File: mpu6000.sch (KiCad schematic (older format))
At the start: 4 parts, among them U3 MPU-6000

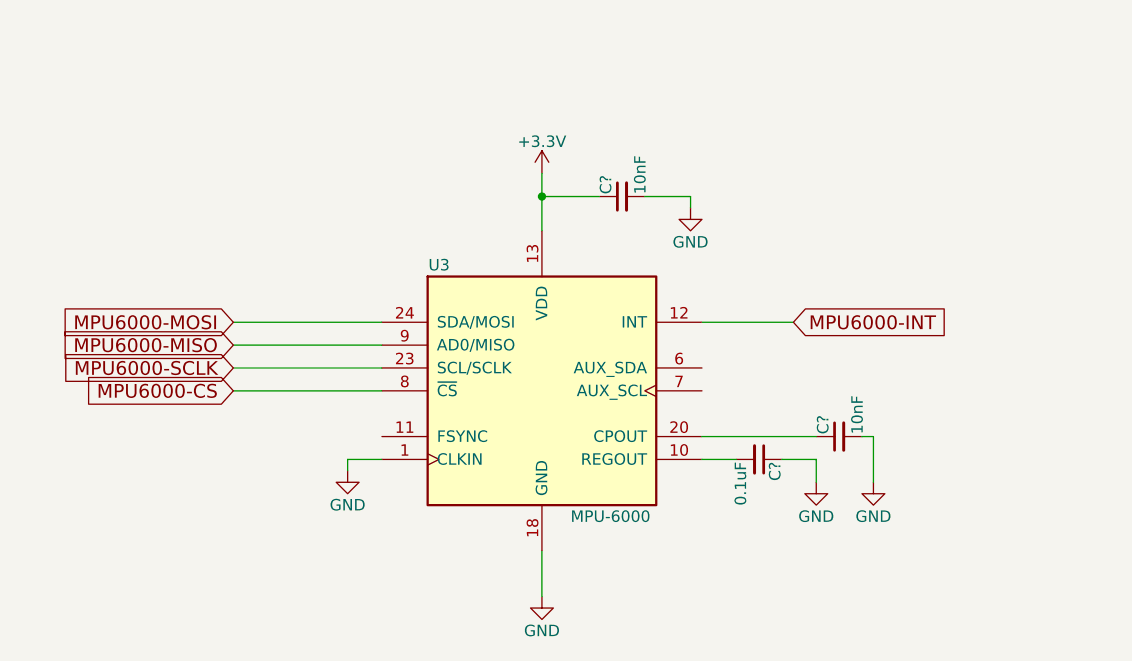
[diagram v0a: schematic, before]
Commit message: Moved LEDs to new sheet
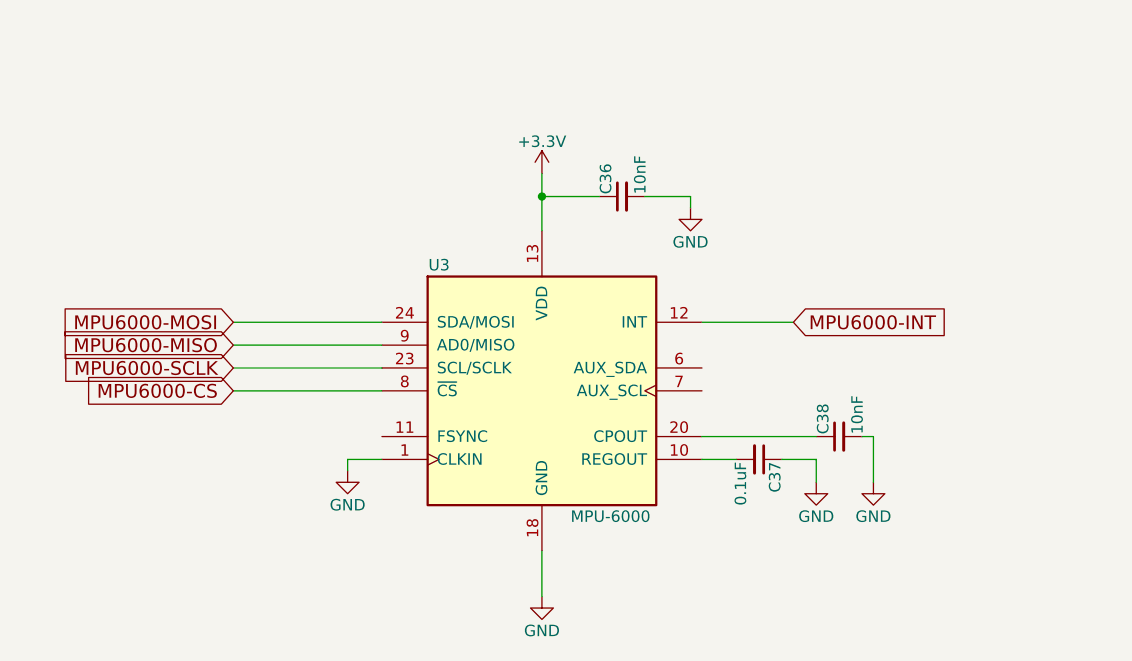
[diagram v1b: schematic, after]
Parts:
- gave numbers to parts that had none: 3
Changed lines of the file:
@@
 $Descr A4 11693 8268
 encoding utf-8
-Sheet 4 5
+Sheet 4 6
 Title ""
 Date ""
@@
 	7050 3500 6650 3500
 $Comp
-L +3.3V #PWR?
+L +3.3V #PWR1242
 U 1 1 5B360D5D
 P 5950 2850
-F 0 "#PWR?" H 5950 2700 50  0001 C CNN
+F 0 "#PWR1242" H 5950 2700 50  0001 C CNN
 F 1 "+3.3V" H 5950 2990 50  0000 C CNN
 F 2 "" H 5950 2850 50  0001 C CNN
@@
 $EndComp
 $Comp
-L GND #PWR?
+L GND #PWR1243
 U 1 1 5B360D77
 P 5950 4700
-F 0 "#PWR?" H 5950 4450 50  0001 C CNN
+F 0 "#PWR1243" H 5950 4450 50  0001 C CNN
 F 1 "GND" H 5950 4550 50  0000 C CNN
 F 2 "" H 5950 4700 50  0001 C CNN
@@
 	5950 2850 5950 3100
 $Comp
-L GND #PWR?
+L GND #PWR1246
 U 1 1 5B360DB0
 P 7400 4200
-F 0 "#PWR?" H 7400 3950 50  0001 C CNN
+F 0 "#PWR1246" H 7400 3950 50  0001 C CNN
 F 1 "GND" H 7400 4050 50  0000 C CNN
 F 2 "" H 7400 4200 50  0001 C CNN
@@
 $EndComp
 $Comp
-L GND #PWR?
+L GND #PWR1245
 U 1 1 5B360DCD
 P 7150 4200
-F 0 "#PWR?" H 7150 3950 50  0001 C CNN
+F 0 "#PWR1245" H 7150 3950 50  0001 C CNN
 F 1 "GND" H 7150 4050 50  0000 C CNN
 F 2 "" H 7150 4200 50  0001 C CNN
@@
 $EndComp
 $Comp
-L C_Small C?
+L C_Small C37
 U 1 1 5B360DDD
 P 6900 4100
-F 0 "C?" H 6910 4170 50  0000 L CNN
+F 0 "C37" H 6910 4170 50  0000 L CNN
 F 1 "0.1uF" H 6910 4020 50  0000 L CNN
 F 2 "" H 6900 4100 50  0001 C CNN
@@
 $EndComp
 $Comp
-L C_Small C?
+L C_Small C38
 U 1 1 5B360E5E
 P 7250 4000
-F 0 "C?" H 7260 4070 50  0000 L CNN
+F 0 "C38" H 7260 4070 50  0000 L CNN
 F 1 "10nF" H 7260 3920 50  0000 L CNN
 F 2 "" H 7250 4000 50  0001 C CNN
@@
 	7150 4100 7150 4200
 $Comp
-L C_Small C?
+L C_Small C36
 U 1 1 5B361055
 P 6300 2950
-F 0 "C?" H 6310 3020 50  0000 L CNN
+F 0 "C36" H 6310 3020 50  0000 L CNN
 F 1 "10nF" H 6310 2870 50  0000 L CNN
 F 2 "" H 6300 2950 50  0001 C CNN
@@
 $EndComp
 $Comp
-L GND #PWR?
+L GND #PWR1244
 U 1 1 5B3610B5
 P 6600 3000
-F 0 "#PWR?" H 6600 2750 50  0001 C CNN
+F 0 "#PWR1244" H 6600 2750 50  0001 C CNN
 F 1 "GND" H 6600 2850 50  0000 C CNN
 F 2 "" H 6600 3000 50  0001 C CNN
@@
 	6600 2950 6600 3000
 $Comp
-L GND #PWR?
+L GND #PWR1241
 U 1 1 5B3610F5
 P 5100 4150
-F 0 "#PWR?" H 5100 3900 50  0001 C CNN
+F 0 "#PWR1241" H 5100 3900 50  0001 C CNN
 F 1 "GND" H 5100 4000 50  0000 C CNN
 F 2 "" H 5100 4150 50  0001 C CNN

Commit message: zone movement + routing of all circuits
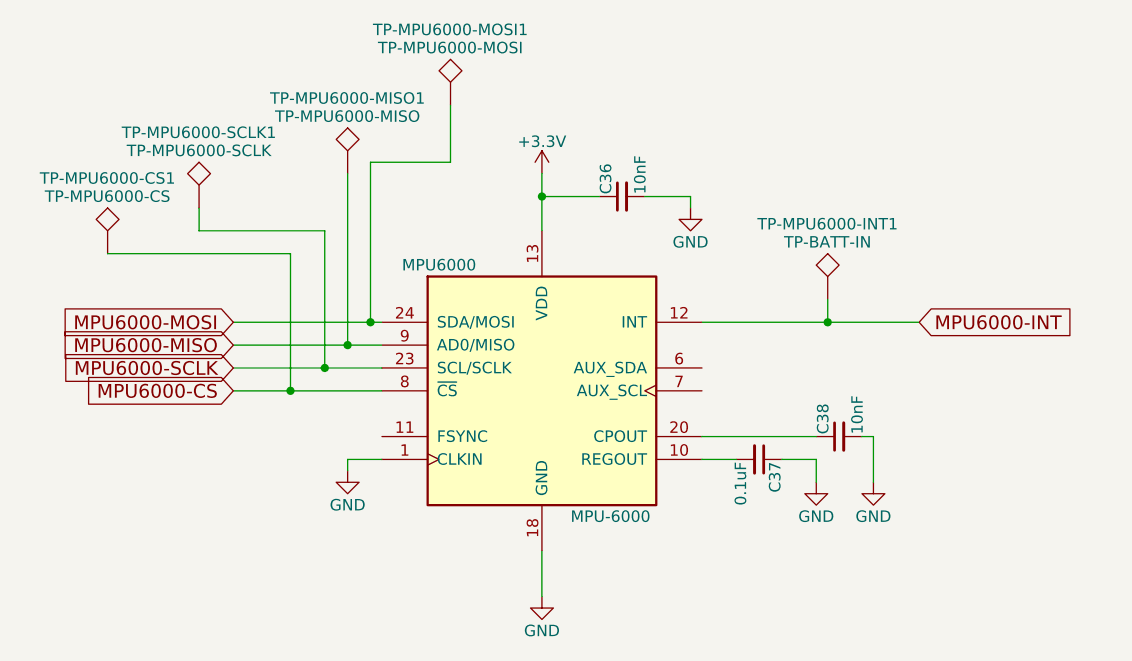
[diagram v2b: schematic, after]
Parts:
- added TP-MPU6000-CS1: TP-MPU6000-CS, Measurement_Points:Measurement_Point_Round-SMD-Pad_Small, symbol TEST
- added TP-MPU6000-INT1: TP-BATT-IN, Measurement_Points:Measurement_Point_Round-SMD-Pad_Small, symbol TEST
- added TP-MPU6000-MISO1: TP-MPU6000-MISO, Measurement_Points:Measurement_Point_Round-SMD-Pad_Small, symbol TEST
- added TP-MPU6000-MOSI1: TP-MPU6000-MOSI, Measurement_Points:Measurement_Point_Round-SMD-Pad_Small, symbol TEST
- added TP-MPU6000-SCLK1: TP-MPU6000-SCLK, Measurement_Points:Measurement_Point_Round-SMD-Pad_Small, symbol TEST
- C36, C37, C38: footprint (none) -> Capacitors_SMD:C_0603
- renumbered U3 to MPU6000
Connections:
- net MPU6000-CS: now also TP-MPU6000-CS1.1
- net MPU6000-INT: now also TP-MPU6000-INT1.1
- net MPU6000-MISO: now also TP-MPU6000-MISO1.1
- net MPU6000-MOSI: now also TP-MPU6000-MOSI1.1
- net MPU6000-SCLK: now also TP-MPU6000-SCLK1.1
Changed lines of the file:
@@
 EESchema Schematic File Version 2
 LIBS:power
-LIBS:device
 LIBS:transistors
 LIBS:conn
@@
 LIBS:sensors
 LIBS:dc-dc
+LIBS:device
 LIBS:dc26-cache
 EELAYER 25 0
@@
 $Descr A4 11693 8268
 encoding utf-8
-Sheet 4 6
+Sheet 3 6
 Title ""
 Date ""
@@
 $EndDescr
 $Comp
-L MPU-6000 U3
+L MPU-6000 MPU6000
 U 1 1 5B2F4E9F
 P 5950 3800
-F 0 "U3" H 5500 4350 50  0000 C CNN
+F 0 "MPU6000" H 5500 4350 50  0000 C CNN
 F 1 "MPU-6000" H 6250 3250 50  0000 C CNN
 F 2 "Housings_DFN_QFN:QFN-24-1EP_4x4mm_Pitch0.5mm" H 5950 3000 50  0001 C CNN
@@
 Wire Wire Line
 	4600 3800 5250 3800
-Text GLabel 7050 3500 2    60   Input ~ 0
+Text GLabel 7600 3500 2    60   Input ~ 0
 MPU6000-INT
 Wire Wire Line
-	7050 3500 6650 3500
-$Comp
-L +3.3V #PWR1242
+	6650 3500 7600 3500
+$Comp
+L +3.3V #PWR037
 U 1 1 5B360D5D
 P 5950 2850
-F 0 "#PWR1242" H 5950 2700 50  0001 C CNN
+F 0 "#PWR037" H 5950 2700 50  0001 C CNN
 F 1 "+3.3V" H 5950 2990 50  0000 C CNN
 F 2 "" H 5950 2850 50  0001 C CNN
@@
 $EndComp
 $Comp
-L GND #PWR1243
+L GND #PWR038
 U 1 1 5B360D77
 P 5950 4700
-F 0 "#PWR1243" H 5950 4450 50  0001 C CNN
+F 0 "#PWR038" H 5950 4450 50  0001 C CNN
 F 1 "GND" H 5950 4550 50  0000 C CNN
 F 2 "" H 5950 4700 50  0001 C CNN
@@
 	5950 2850 5950 3100
 $Comp
-L GND #PWR1246
+L GND #PWR039
 U 1 1 5B360DB0
 P 7400 4200
-F 0 "#PWR1246" H 7400 3950 50  0001 C CNN
+F 0 "#PWR039" H 7400 3950 50  0001 C CNN
 F 1 "GND" H 7400 4050 50  0000 C CNN
 F 2 "" H 7400 4200 50  0001 C CNN
@@
 $EndComp
 $Comp
-L GND #PWR1245
+L GND #PWR040
 U 1 1 5B360DCD
 P 7150 4200
-F 0 "#PWR1245" H 7150 3950 50  0001 C CNN
+F 0 "#PWR040" H 7150 3950 50  0001 C CNN
 F 1 "GND" H 7150 4050 50  0000 C CNN
 F 2 "" H 7150 4200 50  0001 C CNN
@@
 F 0 "C37" H 6910 4170 50  0000 L CNN
 F 1 "0.1uF" H 6910 4020 50  0000 L CNN
-F 2 "" H 6900 4100 50  0001 C CNN
+F 2 "Capacitors_SMD:C_0603" H 6900 4100 50  0001 C CNN
 F 3 "" H 6900 4100 50  0001 C CNN
 	1    6900 4100
@@
 F 0 "C38" H 7260 4070 50  0000 L CNN
 F 1 "10nF" H 7260 3920 50  0000 L CNN
-F 2 "" H 7250 4000 50  0001 C CNN
+F 2 "Capacitors_SMD:C_0603" H 7250 4000 50  0001 C CNN
 F 3 "" H 7250 4000 50  0001 C CNN
 	1    7250 4000
@@
 F 0 "C36" H 6310 3020 50  0000 L CNN
 F 1 "10nF" H 6310 2870 50  0000 L CNN
-F 2 "" H 6300 2950 50  0001 C CNN
+F 2 "Capacitors_SMD:C_0603" H 6300 2950 50  0001 C CNN
 F 3 "" H 6300 2950 50  0001 C CNN
 	1    6300 2950
@@
 $EndComp
 $Comp
-L GND #PWR1244
+L GND #PWR041
 U 1 1 5B3610B5
 P 6600 3000
-F 0 "#PWR1244" H 6600 2750 50  0001 C CNN
+F 0 "#PWR041" H 6600 2750 50  0001 C CNN
 F 1 "GND" H 6600 2850 50  0000 C CNN
 F 2 "" H 6600 3000 50  0001 C CNN
@@
 	6600 2950 6600 3000
 $Comp
-L GND #PWR1241
+L GND #PWR042
 U 1 1 5B3610F5
 P 5100 4150
-F 0 "#PWR1241" H 5100 3900 50  0001 C CNN
+F 0 "#PWR042" H 5100 3900 50  0001 C CNN
 F 1 "GND" H 5100 4000 50  0000 C CNN
 F 2 "" H 5100 4150 50  0001 C CNN
@@
 Wire Wire Line
 	5100 4100 5100 4150
+$Comp
+L TEST TP-MPU6000-CS1
+U 1 1 5B3F20EC
+P 4050 3200
+F 0 "TP-MPU6000-CS1" H 4050 3500 50  0000 C BNN
+F 1 "TP-MPU6000-CS" H 4050 3450 50  0000 C CNN
+F 2 "Measurement_Points:Measurement_Point_Round-SMD-Pad_Small" H 4050 3200 50  0001 C CNN
+F 3 "" H 4050 3200 50  0001 C CNN
+	1    4050 3200
+	1    0    0    -1
+$EndComp
+$Comp
+L TEST TP-MPU6000-SCLK1
+U 1 1 5B3F20FE
+P 4450 3000
+F 0 "TP-MPU6000-SCLK1" H 4450 3300 50  0000 C BNN
+F 1 "TP-MPU6000-SCLK" H 4450 3250 50  0000 C CNN
+F 2 "Measurement_Points:Measurement_Point_Round-SMD-Pad_Small" H 4450 3000 50  0001 C CNN
+F 3 "" H 4450 3000 50  0001 C CNN
+	1    4450 3000
+	1    0    0    -1
+$EndComp
+$Comp
+L TEST TP-MPU6000-MISO1
+U 1 1 5B3F2136
+P 5100 2850
+F 0 "TP-MPU6000-MISO1" H 5100 3150 50  0000 C BNN
+F 1 "TP-MPU6000-MISO" H 5100 3100 50  0000 C CNN
+F 2 "Measurement_Points:Measurement_Point_Round-SMD-Pad_Small" H 5100 2850 50  0001 C CNN
+F 3 "" H 5100 2850 50  0001 C CNN
+	1    5100 2850
+	1    0    0    -1
+$EndComp
+$Comp
+L TEST TP-MPU6000-MOSI1
+U 1 1 5B3F216D
+P 5550 2550
+F 0 "TP-MPU6000-MOSI1" H 5550 2850 50  0000 C BNN
+F 1 "TP-MPU6000-MOSI" H 5550 2800 50  0000 C CNN
+F 2 "Measurement_Points:Measurement_Point_Round-SMD-Pad_Small" H 5550 2550 50  0001 C CNN
+F 3 "" H 5550 2550 50  0001 C CNN
+	1    5550 2550
+	1    0    0    -1
+$EndComp
+$Comp
+L TEST TP-MPU6000-INT1
+U 1 1 5B3F2199
+P 7200 3400
+F 0 "TP-MPU6000-INT1" H 7200 3700 50  0000 C BNN
+F 1 "TP-BATT-IN" H 7200 3650 50  0000 C CNN
+F 2 "Measurement_Points:Measurement_Point_Round-SMD-Pad_Small" H 7200 3400 50  0001 C CNN
+F 3 "" H 7200 3400 50  0001 C CNN
+	1    7200 3400
+	1    0    0    -1
+$EndComp
+Wire Wire Line
+	7200 3400 7200 3500
+Connection ~ 7200 3500
+Wire Wire Line
+	5200 2800 5200 3500
+Connection ~ 5200 3500
+Wire Wire Line
+	5100 2850 5100 3600
+Connection ~ 5100 3600
+Wire Wire Line
+	4450 3000 4450 3100
+Wire Wire Line
+	4450 3100 5000 3100
+Wire Wire Line
+	5000 3100 5000 3700
+Connection ~ 5000 3700
+Wire Wire Line
+	4050 3200 4850 3200
+Wire Wire Line
+	4850 3200 4850 3800
+Connection ~ 4850 3800
+Wire Wire Line
+	5550 2550 5550 2800
+Wire Wire Line
+	5550 2800 5200 2800
 $EndSCHEMATC

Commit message: pcb layout
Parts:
- TP-MPU6000-INT1: value TP-BATT-IN -> TP-MPU6000-INT1
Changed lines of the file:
@@
 P 7200 3400
 F 0 "TP-MPU6000-INT1" H 7200 3700 50  0000 C BNN
-F 1 "TP-BATT-IN" H 7200 3650 50  0000 C CNN
+F 1 "TP-MPU6000-INT1" H 7200 3650 50  0000 C CNN
 F 2 "Measurement_Points:Measurement_Point_Round-SMD-Pad_Small" H 7200 3400 50  0001 C CNN
 F 3 "" H 7200 3400 50  0001 C CNN

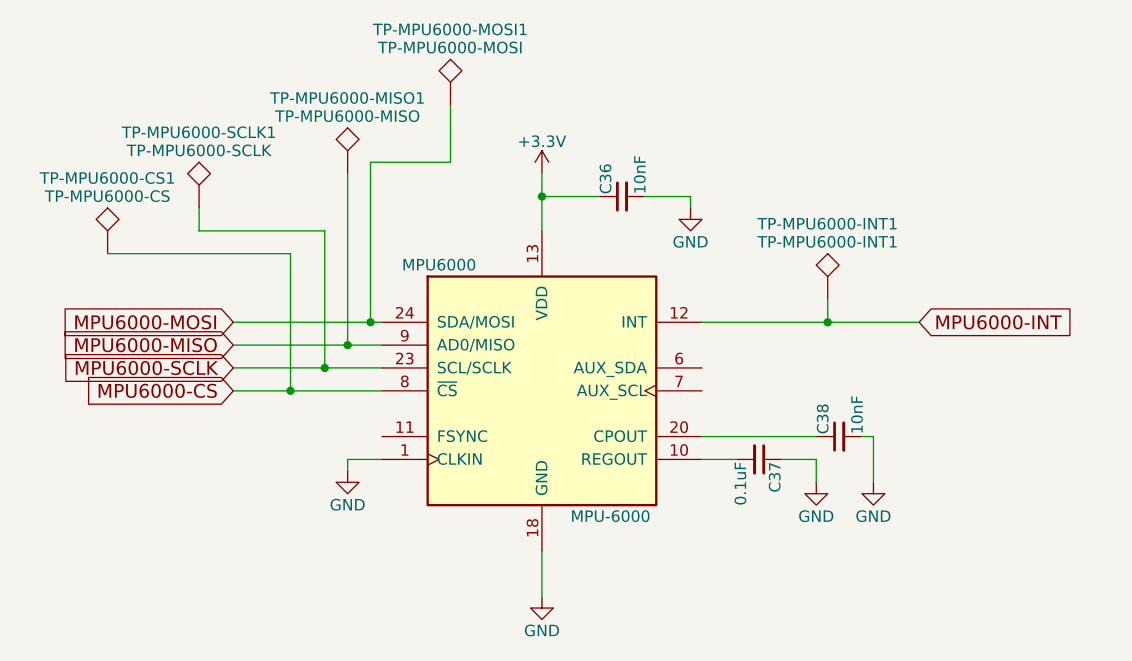
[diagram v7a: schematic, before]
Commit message: Changing tp silkscreen names
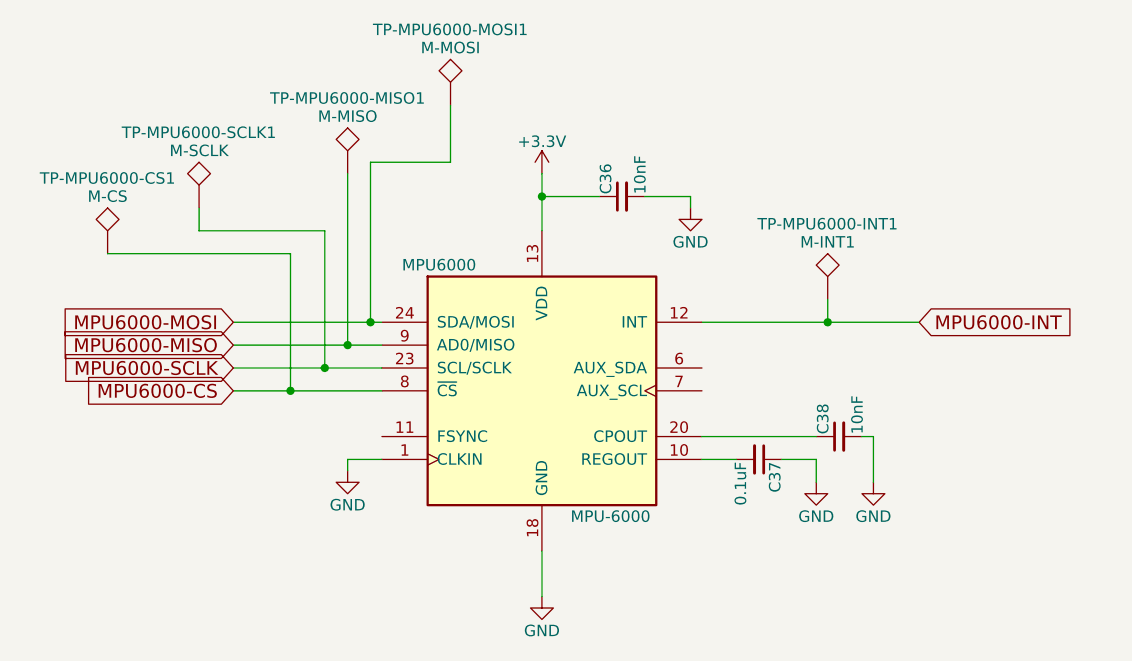
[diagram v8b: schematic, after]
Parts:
- TP-MPU6000-CS1: value TP-MPU6000-CS -> M-CS
- TP-MPU6000-INT1: value TP-MPU6000-INT1 -> M-INT1
- TP-MPU6000-MISO1: value TP-MPU6000-MISO -> M-MISO
- TP-MPU6000-MOSI1: value TP-MPU6000-MOSI -> M-MOSI
- TP-MPU6000-SCLK1: value TP-MPU6000-SCLK -> M-SCLK
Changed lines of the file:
@@
 $Descr A4 11693 8268
 encoding utf-8
-Sheet 3 6
+Sheet 3 7
 Title ""
 Date ""
@@
 	6650 3500 7600 3500
 $Comp
-L +3.3V #PWR042
+L +3.3V #PWR38
 U 1 1 5B360D5D
 P 5950 2850
-F 0 "#PWR042" H 5950 2700 50  0001 C CNN
+F 0 "#PWR38" H 5950 2700 50  0001 C CNN
 F 1 "+3.3V" H 5950 2990 50  0000 C CNN
 F 2 "" H 5950 2850 50  0001 C CNN
@@
 $EndComp
 $Comp
-L GND #PWR043
+L GND #PWR39
 U 1 1 5B360D77
 P 5950 4700
-F 0 "#PWR043" H 5950 4450 50  0001 C CNN
+F 0 "#PWR39" H 5950 4450 50  0001 C CNN
 F 1 "GND" H 5950 4550 50  0000 C CNN
 F 2 "" H 5950 4700 50  0001 C CNN
@@
 	5950 2850 5950 3100
 $Comp
-L GND #PWR044
+L GND #PWR42
 U 1 1 5B360DB0
 P 7400 4200
-F 0 "#PWR044" H 7400 3950 50  0001 C CNN
+F 0 "#PWR42" H 7400 3950 50  0001 C CNN
 F 1 "GND" H 7400 4050 50  0000 C CNN
 F 2 "" H 7400 4200 50  0001 C CNN
@@
 $EndComp
 $Comp
-L GND #PWR045
+L GND #PWR41
 U 1 1 5B360DCD
 P 7150 4200
-F 0 "#PWR045" H 7150 3950 50  0001 C CNN
+F 0 "#PWR41" H 7150 3950 50  0001 C CNN
 F 1 "GND" H 7150 4050 50  0000 C CNN
 F 2 "" H 7150 4200 50  0001 C CNN
@@
 $EndComp
 $Comp
-L GND #PWR046
+L GND #PWR40
 U 1 1 5B3610B5
 P 6600 3000
-F 0 "#PWR046" H 6600 2750 50  0001 C CNN
+F 0 "#PWR40" H 6600 2750 50  0001 C CNN
 F 1 "GND" H 6600 2850 50  0000 C CNN
 F 2 "" H 6600 3000 50  0001 C CNN
@@
 	6600 2950 6600 3000
 $Comp
-L GND #PWR047
+L GND #PWR37
 U 1 1 5B3610F5
 P 5100 4150
-F 0 "#PWR047" H 5100 3900 50  0001 C CNN
+F 0 "#PWR37" H 5100 3900 50  0001 C CNN
 F 1 "GND" H 5100 4000 50  0000 C CNN
 F 2 "" H 5100 4150 50  0001 C CNN
@@
 P 4050 3200
 F 0 "TP-MPU6000-CS1" H 4050 3500 50  0000 C BNN
-F 1 "TP-MPU6000-CS" H 4050 3450 50  0000 C CNN
+F 1 "M-CS" H 4050 3450 50  0000 C CNN
 F 2 "Measurement_Points:Measurement_Point_Round-SMD-Pad_Small" H 4050 3200 50  0001 C CNN
 F 3 "" H 4050 3200 50  0001 C CNN
@@
 P 4450 3000
 F 0 "TP-MPU6000-SCLK1" H 4450 3300 50  0000 C BNN
-F 1 "TP-MPU6000-SCLK" H 4450 3250 50  0000 C CNN
+F 1 "M-SCLK" H 4450 3250 50  0000 C CNN
 F 2 "Measurement_Points:Measurement_Point_Round-SMD-Pad_Small" H 4450 3000 50  0001 C CNN
 F 3 "" H 4450 3000 50  0001 C CNN
@@
 P 5100 2850
 F 0 "TP-MPU6000-MISO1" H 5100 3150 50  0000 C BNN
-F 1 "TP-MPU6000-MISO" H 5100 3100 50  0000 C CNN
+F 1 "M-MISO" H 5100 3100 50  0000 C CNN
 F 2 "Measurement_Points:Measurement_Point_Round-SMD-Pad_Small" H 5100 2850 50  0001 C CNN
 F 3 "" H 5100 2850 50  0001 C CNN
@@
 P 5550 2550
 F 0 "TP-MPU6000-MOSI1" H 5550 2850 50  0000 C BNN
-F 1 "TP-MPU6000-MOSI" H 5550 2800 50  0000 C CNN
+F 1 "M-MOSI" H 5550 2800 50  0000 C CNN
 F 2 "Measurement_Points:Measurement_Point_Round-SMD-Pad_Small" H 5550 2550 50  0001 C CNN
 F 3 "" H 5550 2550 50  0001 C CNN
@@
 P 7200 3400
 F 0 "TP-MPU6000-INT1" H 7200 3700 50  0000 C BNN
-F 1 "TP-MPU6000-INT1" H 7200 3650 50  0000 C CNN
+F 1 "M-INT1" H 7200 3650 50  0000 C CNN
 F 2 "Measurement_Points:Measurement_Point_Round-SMD-Pad_Small" H 7200 3400 50  0001 C CNN
 F 3 "" H 7200 3400 50  0001 C CNN
